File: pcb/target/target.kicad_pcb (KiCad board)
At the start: 2 copper layers, 62 x 72.2 mm, 55 parts, among them J1 Pogo_01x06_female, J10 Conn_01x03_Pin, J11 Conn_01x03_Pin, J12 Conn_01x03_Pin, J13 Conn_01x03_Pin, J14 Conn_01x03_Pin, J15 Conn_01x03_Pin, J16 Conn_01x03_Pin, J17 Conn_01x03_Pin, J18 Conn_01x03_Pin, J19 Conn_01x03_Pin, J2 Pogo_01x06_male, J20 Conn_01x03_Pin, J21 Conn_01x03_Pin, J3 Conn_01x03_Pin, J4 Conn_01x03_Pin, J5 Piezo, J6 Conn_01x03_Pin, J7 Conn_01x03_Pin, J8 Conn_01x03_Pin, J9 Conn_01x03_Pin, Q1 SI2333CDS-T1-GE3, U1 ATtiny3216-S

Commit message: finishing up target pcb
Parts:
- J1, J2: footprint Connector_Wire:SolderWire-1sqmm_1x06_P5.4mm_D1.4mm_OD2.7mm -> custom_footprints:01x06 SMD 4x4mm pad
- J10, J11, J12, J13, J14, J15, J16, J17, J18, J19, J20, J21, J6, J7, J8, J9: footprint Connector_Wire:SolderWire-0.25sqmm_1x03_P4.2mm_D0.65mm_OD1.7mm -> custom_footprints:01x03 SMD 2x3mm pad
- J3, J4: footprint Connector_Wire:SolderWire-0.75sqmm_1x03_P4.8mm_D1.25mm_OD2.3mm -> custom_footprints:01x03 SMD 2x3mm pad
- moved J12 192.7 mm to (96.1, 68.0)
- moved D10 189.6 mm to (86.1, 68.0)
- moved D11 187.6 mm to (65.1, 68.0)
- moved C3 187.2 mm to (59.1, 65.6), turned to 90 degrees
- moved J13 186.0 mm to (55.1, 68.0)
- moved J10 174.5 mm to (87.6, 25.1)
- moved D8 173.1 mm to (77.5, 25.1)
- moved J16 171.5 mm to (87.6, 39.4)
- moved D9 171.2 mm to (56.5, 25.1)
- moved D14 169.5 mm to (77.5, 39.4)
- moved J11 168.0 mm to (46.4, 25.1)
- moved D15 167.5 mm to (56.5, 39.4)
- moved J17 164.8 mm to (46.4, 39.4)
- moved J21 118.9 mm to (212.2, 123.7), turned to 45 degrees
- moved C5 110.8 mm to (209.8, 119.7), turned to 180 degrees
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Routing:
- net GND Main: track 105.8 -> 12.7 mm, vias 10 -> 14
- net +5V UPDI: track 118.7 -> 63.6 mm, vias 0 -> 2
- net Net-(D12-VDD): track 100.1 -> 49.3 mm
- net Net-(D8-VDD): track 100.1 -> 49.3 mm
- net Net-(D6-VDD): track 100.1 -> 49.3 mm
- net Net-(D8-VSS): track 76.7 -> 37.3 mm
- net Net-(D6-VSS): track 76.7 -> 37.3 mm
- net Net-(D12-VSS): track 76.7 -> 37.3 mm
- net +5V Main: track 154.1 -> 116.7 mm
- net Net-(Q1-Pad1): track 32.4 -> 4.35 mm
- net SDA: track 71.5 -> 94.8 mm, vias 1 -> 2
- net Net-(D12-DOUT): track 39.9 -> 17.9 mm
- net Net-(D6-DOUT): track 39.9 -> 17.9 mm
- net Net-(D8-DOUT): track 39.9 -> 17.9 mm
- net UPDI pin: track 24.0 -> 38.5 mm
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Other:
- board size 62 x 72.2 mm -> 62.2 x 82.8 mm

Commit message: retraced target pcb
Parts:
- removed JP1: SolderJumper_2_Open, Jumper:SolderJumper-2_P1.3mm_Open_TrianglePad1.0x1.5mm
- moved F1 5.21 mm to (77.0, 138.2), turned to 90 degrees
- moved C1 1.50 mm to (83.8, 134.0)
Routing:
- net +5V Main: track 116.7 -> 259.2 mm
- net GND Main: track 12.7 -> 107.0 mm, vias 14 -> 52
- net Net-(Q1-Pad1): track 4.35 -> 30.8 mm
- net SDA: track 94.8 -> 115.5 mm, vias 2 -> 0
- net SCL: track 74.0 -> 94.0 mm, vias 2 -> 0
- net +5V: track 59.0 -> 61.4 mm
- net +5V UPDI: track 63.6 -> 64.7 mm
- net /LED Circle/VCC: track 70.1 -> 70.8 mm
- removed copper zone on F.Cu, net GND Main
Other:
- board size 62.2 x 82.8 mm -> 63.2 x 82.8 mm

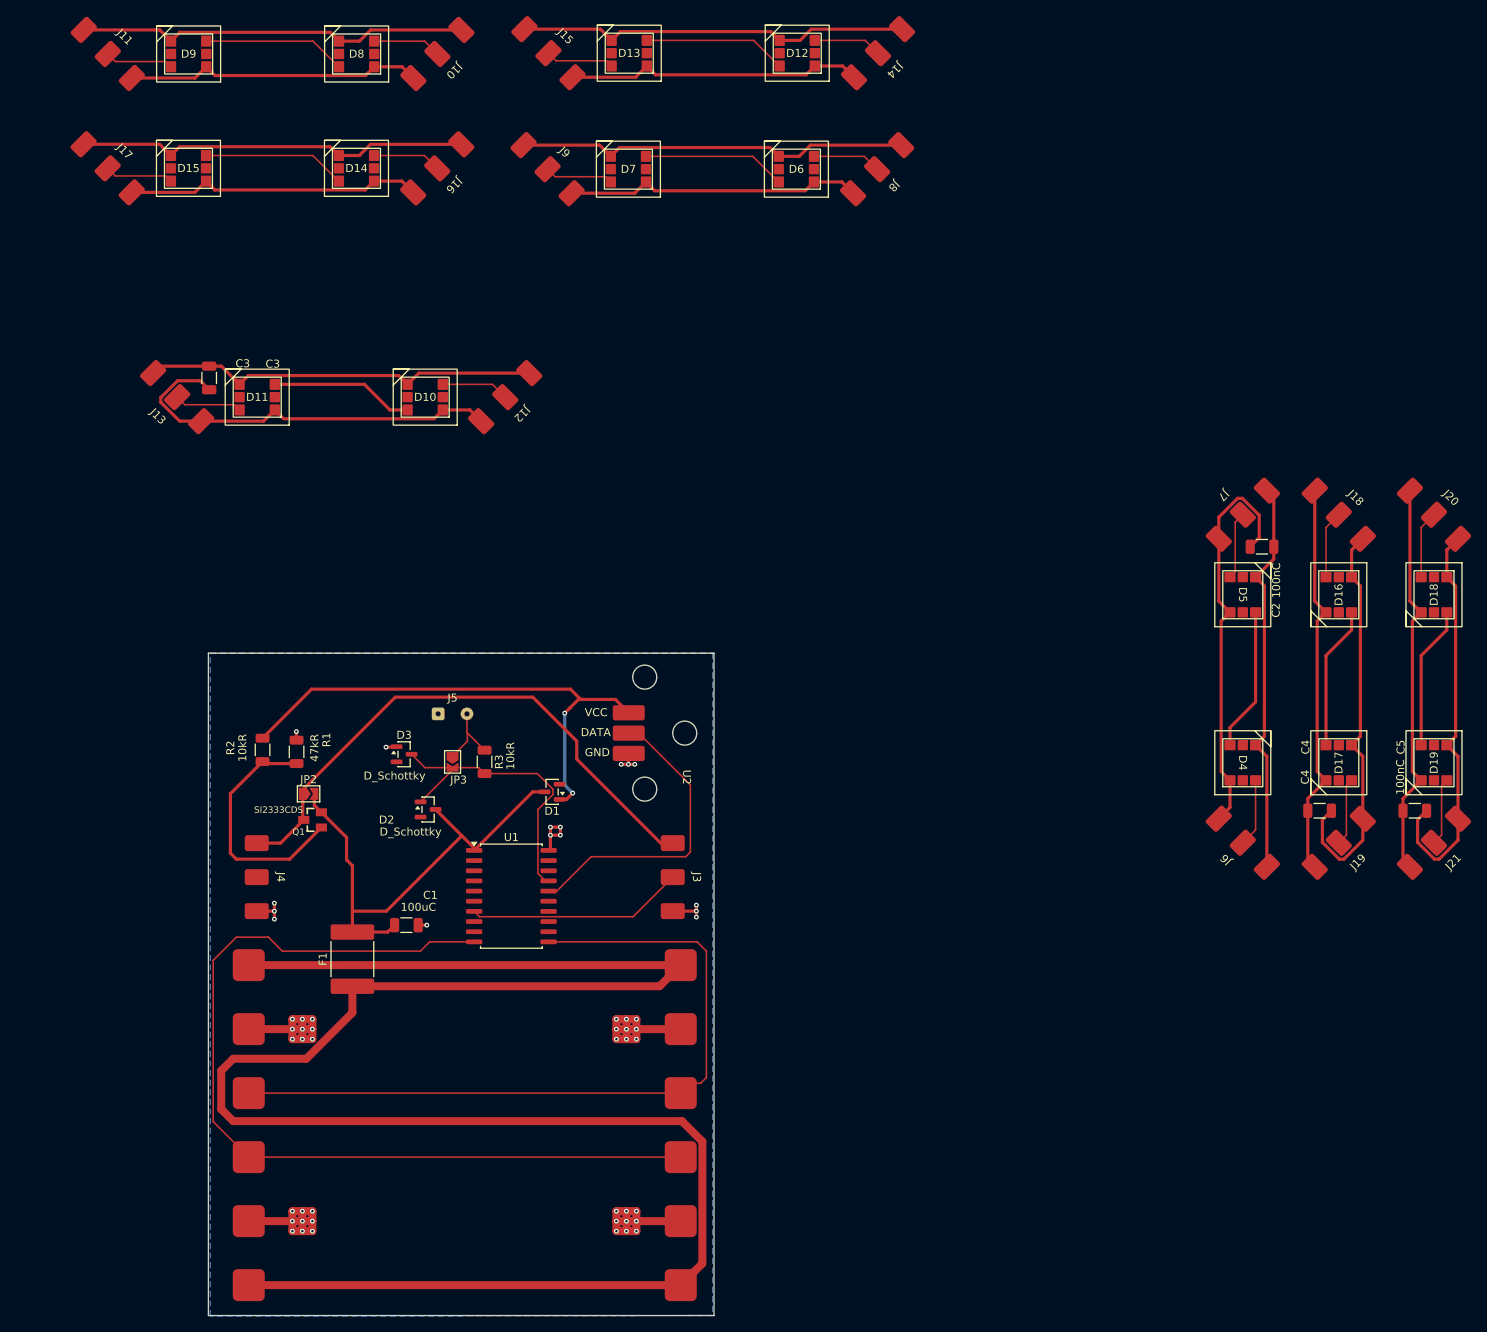
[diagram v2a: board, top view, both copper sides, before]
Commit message: redid target pcb with new components
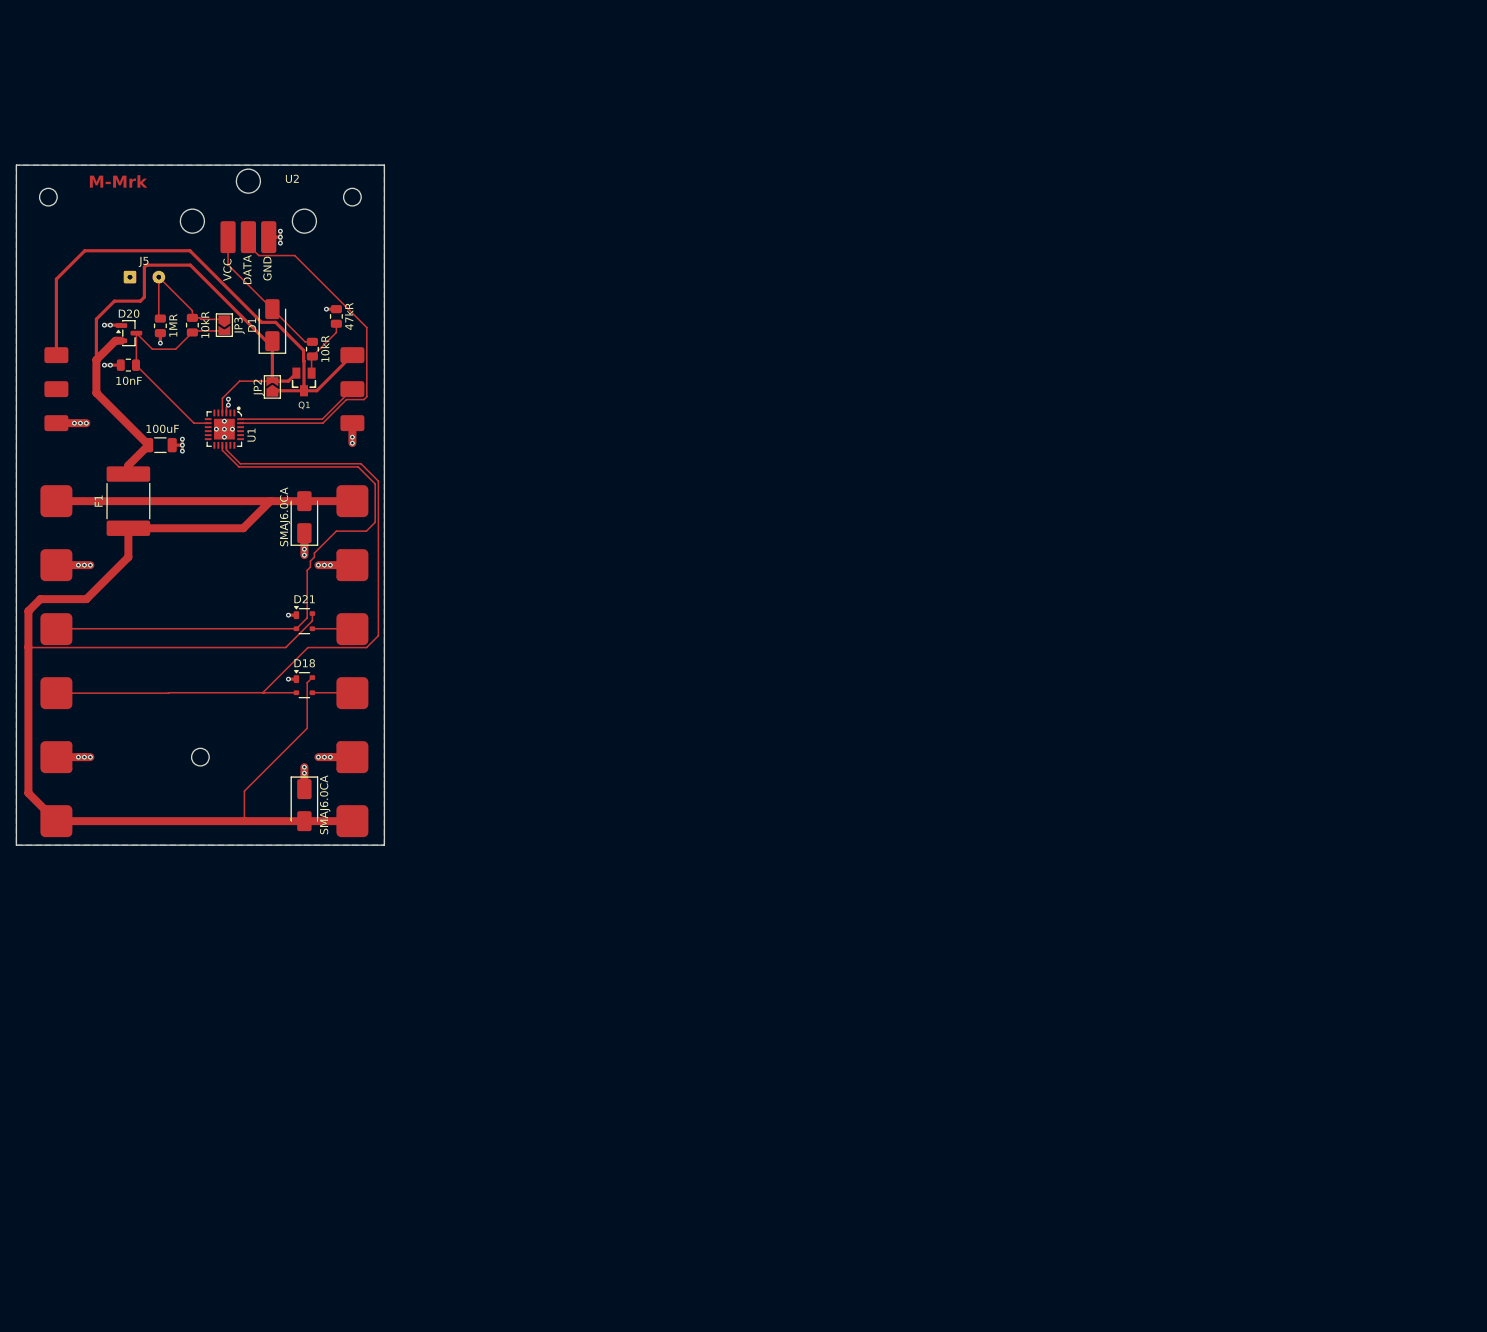
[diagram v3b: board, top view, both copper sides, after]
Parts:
- removed C1: 100uC, Capacitor_SMD:C_1206_3216Metric
- removed C2, C3, C4, C5: 100nC, Capacitor_SMD:C_1206_3216Metric
- removed D10, D11, D12, D13, D14, D15, D16, D17, D19, D4, D5, D6, D7, D8, D9: XL-5050RGBC-SK6812B, custom_footprints:XL-5050RGBC-SK6812B
- removed D2, D3: D_Schottky, custom_footprints:BAT54_SOT23
- removed J10, J11, J12, J13, J14, J15, J16, J17, J18, J19, J20, J21, J6, J7, J8, J9: Conn_01x03_Pin, custom_footprints:01x03 SMD 2x3mm pad
- removed R1: 47kR, Resistor_SMD:R_1206_3216Metric
- removed R2, R3: 10kR, Resistor_SMD:R_1206_3216Metric
- added 100uF: 100u, Capacitor_SMD:C_1206_3216Metric, F.Cu at (53.0, 74.0)
- added 10kR: 10kR, Resistor_SMD:R_0805_2012Metric, F.Cu at (72.0, 62.0)
- added 10kR: 10kR, Resistor_SMD:R_0805_2012Metric, F.Cu at (57.0, 59.0)
- added 10nF: 10n, Capacitor_SMD:C_0805_2012Metric, F.Cu at (49.0, 64.0)
- added 1MR: 1M, Resistor_SMD:R_0805_2012Metric, F.Cu at (53.0, 59.1)
- added 47kR: 47kR, Resistor_SMD:R_0805_2012Metric, F.Cu at (75.0, 57.9)
- added D20: BAT54S, Package_TO_SOT_SMD:SOT-23, F.Cu at (49.1, 60.0)
- added D21: PRTR5V0U2X, Package_TO_SOT_SMD:SOT-143, F.Cu at (71.0, 96.0)
- added REF**: MountingHole_2.2mm_M2, MountingHole:MountingHole_2.2mm_M2, F.Cu at (77.0, 43.0)
- added REF**: MountingHole_2.2mm_M2, MountingHole:MountingHole_2.2mm_M2, F.Cu at (39.0, 43.0)
- added REF**: MountingHole_2.2mm_M2, MountingHole:MountingHole_2.2mm_M2, F.Cu at (58.0, 113.0)
- added SMAJ6.0CA: SMAJ6.0CA, Diode_SMD:D_SMA, F.Cu at (71.0, 119.0)
- added SMAJ6.0CA: SMAJ6.0CA, Diode_SMD:D_SMA, F.Cu at (71.0, 83.0)
- D1: value D_Schottky -> SS54; footprint custom_footprints:BAT54_SOT23 -> Diode_SMD:D_SMA
- D18: value XL-5050RGBC-SK6812B -> PRTR5V0U2X; footprint custom_footprints:XL-5050RGBC-SK6812B -> Package_TO_SOT_SMD:SOT-143
- Q1: value SI2333CDS-T1-GE3 -> SI2333CDS-HXY
- U1: value ATtiny3216-S -> ~; footprint Package_SO:SOIC-20W_7.5x12.8mm_P1.27mm -> custom_footprints:WQFN-24_L4.0-W4.0-P0.50-TL-EP2.6
- moved D18 141.7 mm to (71.0, 104.0), turned to 0 degrees
- moved U2 78.1 mm to (64.0, 48.0), turned to 0 degrees
- moved J3 73.0 mm to (77.0, 67.0)
- moved J2 71.1 mm to (77.0, 101.0), turned to -90 degrees
- moved U1 68.5 mm to (61.0, 72.0), turned to -90 degrees
- moved D1 68.0 mm to (67.0, 59.0), turned to 90 degrees
- moved J5 66.8 mm to (49.2, 53.0)
- moved J4 65.9 mm to (40.0, 67.0)
- moved F1 63.7 mm to (49.0, 81.0)
- moved J1 62.8 mm to (40.0, 101.0), turned to -90 degrees
- moved JP3 61.6 mm to (61.0, 59.0)
- moved Q1 54.8 mm to (71.0, 66.1), turned to 180 degrees
- moved JP2 51.1 mm to (67.0, 66.7), turned to 90 degrees
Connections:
- D18 pad 1: Net-(D18-VDD) -> GND Main
- D18 pad 2: (no net) -> SCL
- D18 pad 3: Net-(D18-DOUT) -> /ESD/SCL OUT
- D18 pad 4: Net-(D18-VSS) -> +5V Main
- J2 pad 3: SDA -> /ESD/SDA OUT
- J2 pad 4: SCL -> /ESD/SCL OUT
- U1 pad 1: +5V -> unconnected-(U1-PA2-Pad1)
- U1 pad 10: SDA -> unconnected-(U1-PB6-Pad10)
- U1 pad 11: SCL -> unconnected-(U1-PB5-Pad11)
- U1 pad 15: unconnected-(U1-PC3-Pad15) -> SDA
- U1 pad 16: UPDI pin -> SCL
- U1 pad 17: Piezo -> unconnected-(U1-PC0-Pad17)
- U1 pad 20: GND Main -> unconnected-(U1-PC3-Pad20)
- U1 pad 3: unconnected-(U1-PA5-Pad3) -> GND Main
- U1 pad 4: unconnected-(U1-PA6-Pad4) -> +5V
- U1 pad 7: LED data -> unconnected-(U1-PA6-Pad7)
- U1 pad 8: unconnected-(U1-PB3-Pad8) -> Piezo
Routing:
- net +5V Main: track 259.2 -> 199.0 mm
- net Net-(D10-VSS): track 51.1 -> 0.00 mm
- net Net-(D16-VSS): track 51.1 -> 0.00 mm
- net Net-(D4-VSS): track 51.1 -> 0.00 mm
- net Net-(D18-VSS): track 51.1 -> 0.00 mm
- net Net-(D4-VDD): track 49.8 -> 0.00 mm
- net Net-(D16-VDD): track 49.8 -> 0.00 mm
- net Net-(D10-VDD): track 49.8 -> 0.00 mm
- net Net-(D18-VDD): track 49.8 -> 0.00 mm
- net Net-(D12-VDD): track 49.3 -> 0.00 mm
- net Net-(D8-VDD): track 49.3 -> 0.00 mm
- net Net-(D6-VDD): track 49.3 -> 0.00 mm
- net Net-(D14-VDD): track 49.3 -> 0.00 mm
- net +5V UPDI: track 64.7 -> 18.0 mm, vias 2 -> 0
- net GND Main: track 107.0 -> 64.1 mm, vias 52 -> 42
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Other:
- board size 63.2 x 82.8 mm -> 46 x 85 mm
- board text added: "M-Mrk"
- board text removed: "SI2333CDS"

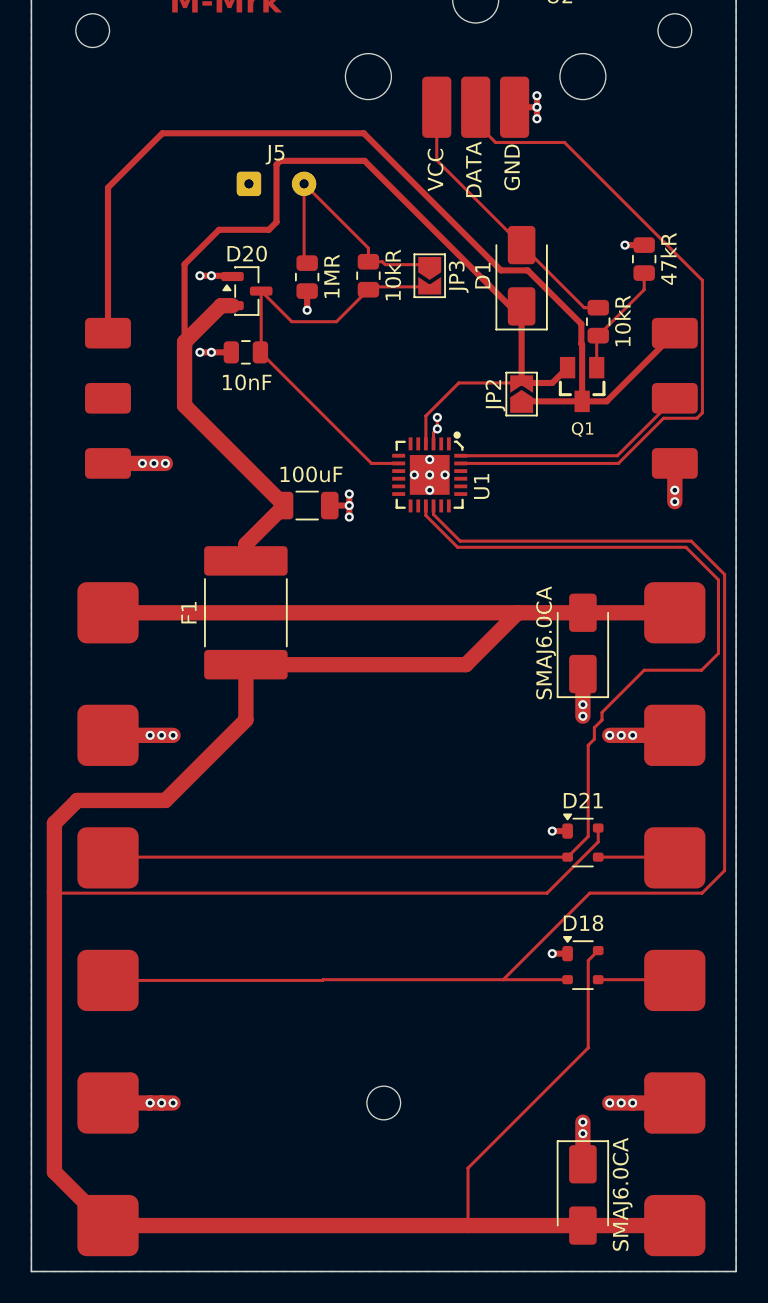
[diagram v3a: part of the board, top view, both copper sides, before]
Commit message: finished all pcbs by adjusting traces acording to 1oz copper weight
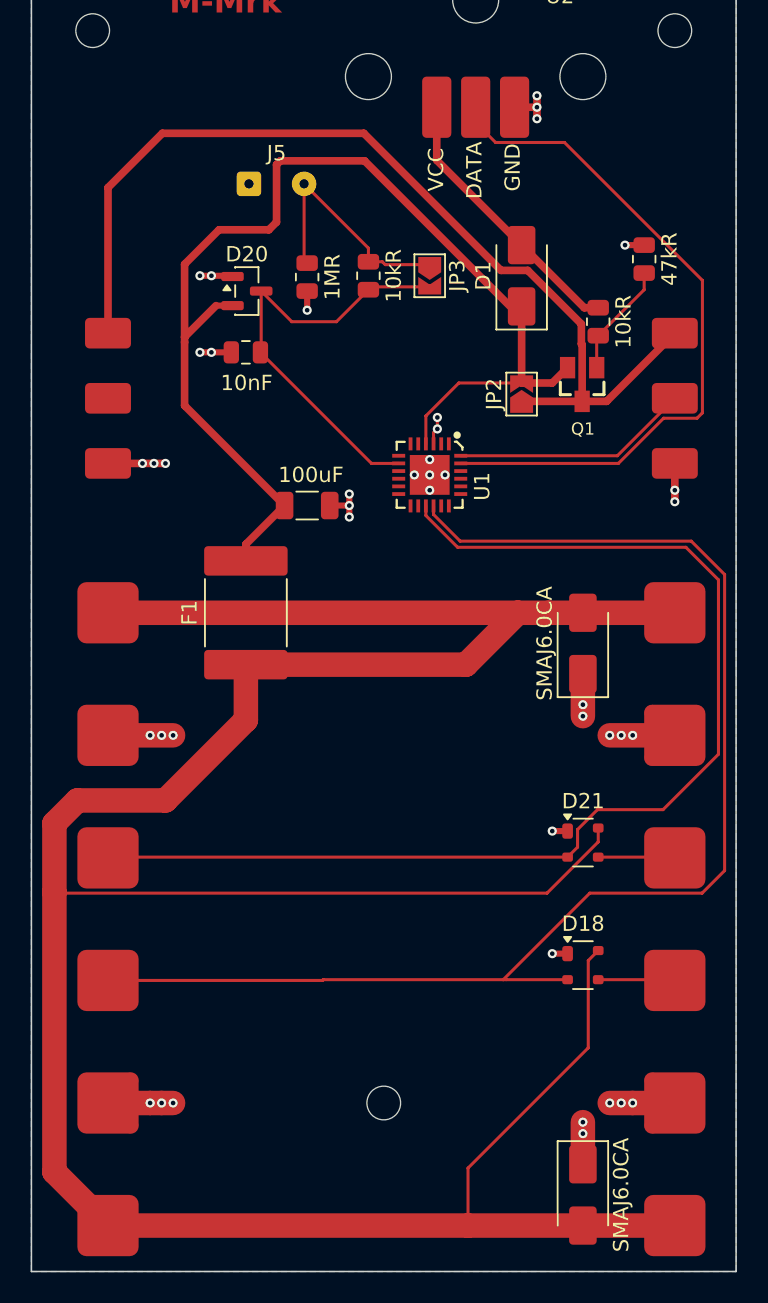
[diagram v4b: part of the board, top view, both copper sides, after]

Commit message: exported all pcbs
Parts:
- moved JP2 1.25 mm to (65.8, 66.7), turned to 180 degrees
- moved Q1 0.68 mm to (71.5, 66.5), turned to 90 degrees
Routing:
- net Net-(Q1-Pad1): track 7.46 -> 22.9 mm
- net +5V: track 75.4 -> 84.9 mm
- net /LED Circle/VCC: track 64.0 -> 57.6 mm
- net UPDI pin: track 45.9 -> 47.5 mm
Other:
- board size 46 x 85 mm -> 46 x 85.8 mm
